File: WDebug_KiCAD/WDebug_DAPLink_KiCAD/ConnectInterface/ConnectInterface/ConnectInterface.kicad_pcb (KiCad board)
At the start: 2 copper layers, 55 x 34 mm, 8 parts, among them J1 Conn_02x05_Counter_Clockwise, J2 Conn_01x20_Female-Connector

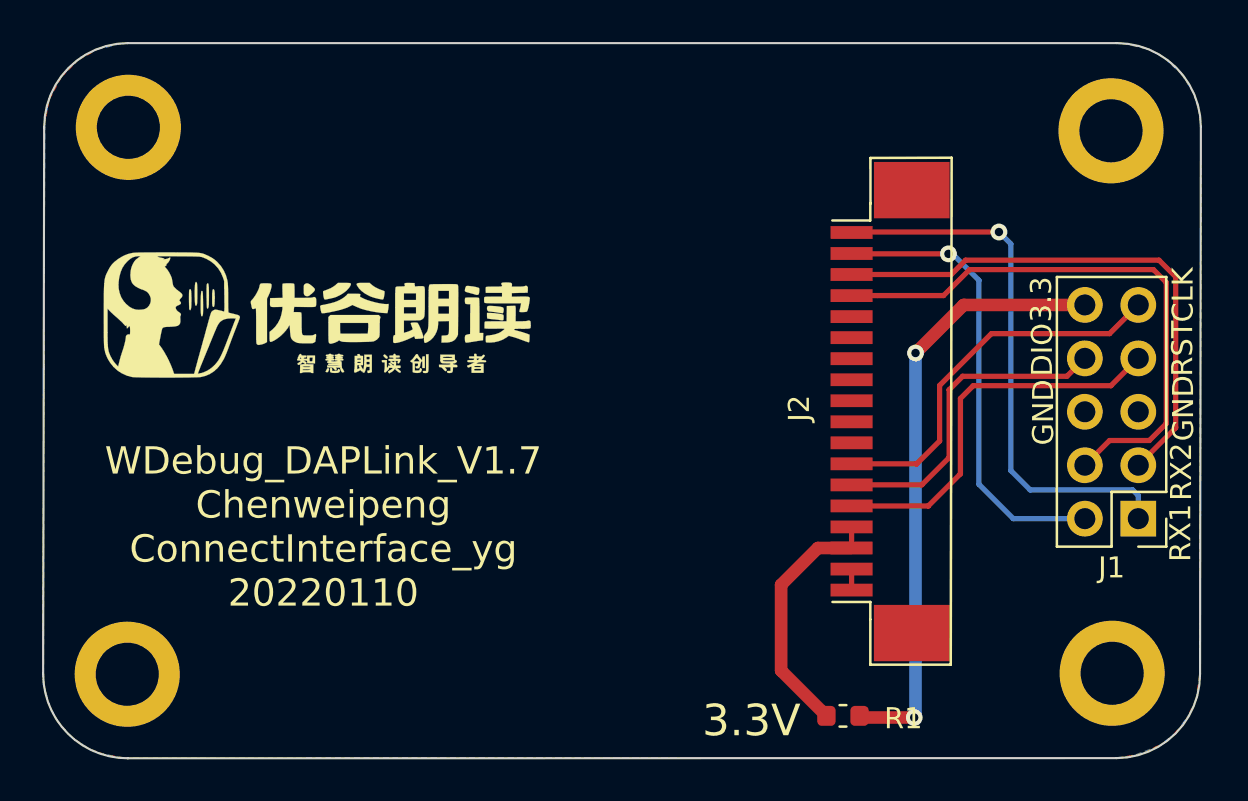
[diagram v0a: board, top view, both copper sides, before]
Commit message: 修改转接板接口定义
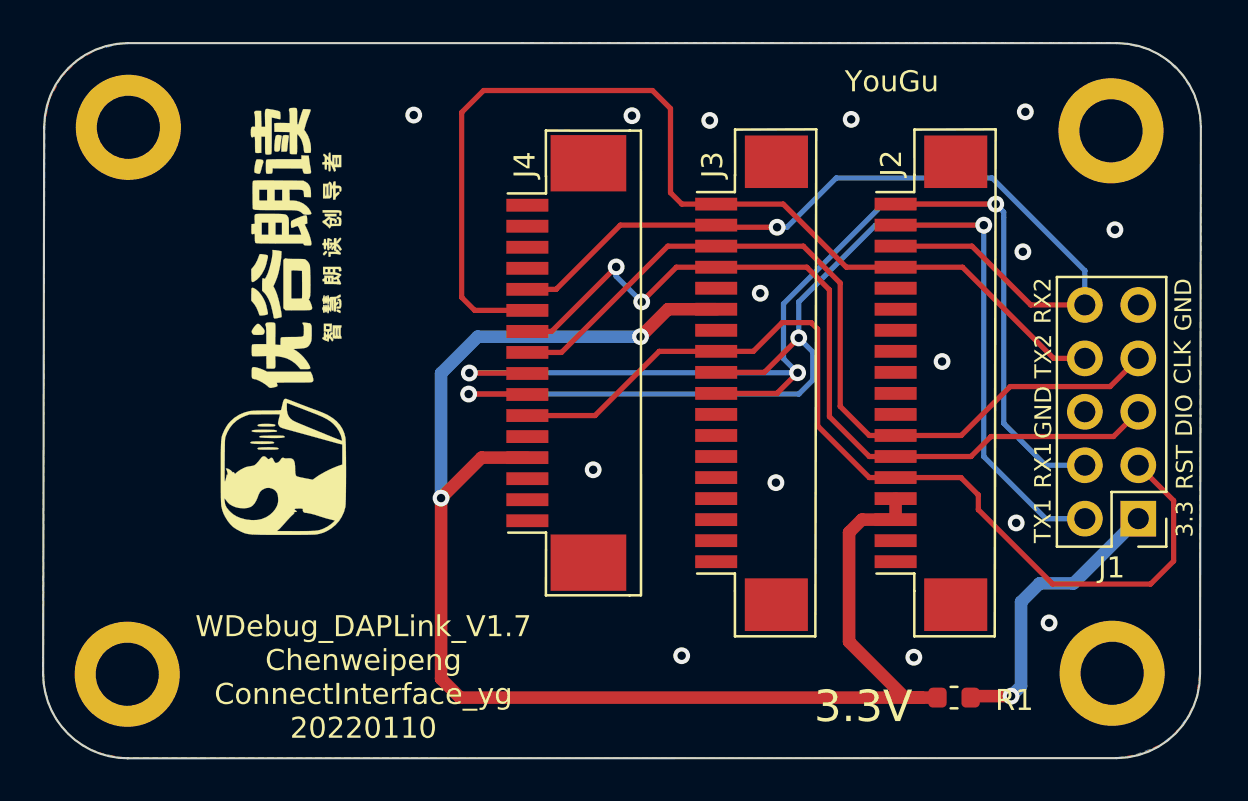
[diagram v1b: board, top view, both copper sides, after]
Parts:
- added J3: Flyaudio18Pin, Connector_PinHeader_1.00mm:1x18_P1.0mm, F.Cu at (166.8, 68.2)
- added J4: Flyaudio16Pin, Connector_PinHeader_1.00mm:1x16_P1.0mm, F.Cu at (154.2, 67.3)
- J1: value Conn_02x05_Counter_Clockwise -> ConnDebug
- J2: value Conn_01x20_Female-Connector -> YOUGU_Debug; footprint WDebug_DAPLink:1x18_P1.0mm -> Connector_PinHeader_1.00mm:1x18_P1.0mm
- moved R1 5.35 mm to (171.8, 83.3)
- moved J2 2.49 mm to (175.3, 68.2)
- moved G*** 2.06 mm to (139.8, 65.1), turned to 90 degrees
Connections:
- net Net-(J2-Pad3) renamed /3_3V
- J1 pad 1: /RX1 -> Net-(J1-Pad1)
- J1 pad 10: Net-(J1-Pad10) -> /RX2
- J1 pad 3: /RX2 -> /TG_RST
- J1 pad 4: /TX2 -> /RX1
- J1 pad 5: GND -> /T_SWDIO
- J1 pad 7: /TG_RST -> /T_SWCLK
- J1 pad 8: /T_SWDIO -> /TX2
- J1 pad 9: /T_SWCLK -> GND
- R1 pad 2: Net-(J1-Pad10) -> Net-(J1-Pad1)
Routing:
- net /3_3V: track 12.2 -> 70.9 mm, vias 0 -> 2
- net /TX1: track 22.0 -> 59.6 mm, vias 1 -> 3
- net /RX1: track 26.2 -> 58.3 mm, vias 1 -> 3
- net Net-(J1-Pad10): track 29.0 -> 0.00 mm, vias 2 -> 0
- net /TG_RST: track 18.6 -> 46.5 mm
- net /T_SWDIO: track 15.5 -> 40.1 mm, vias 0 -> 2
- net /TX2: track 27.2 -> 49.8 mm
- net /T_SWCLK: track 18.3 -> 39.8 mm
- net /RX2: track 25.7 -> 42.4 mm, vias 0 -> 1
- net Net-(J1-Pad1): track 0.00 -> 14.0 mm, vias 0 -> 1
- net GND: track 1.00 -> 0.00 mm, vias 0 -> 15
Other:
- board text added: "TX1"
- board text added: "TX2"
- board text added: "YouGu"

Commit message: 修改V1.7版本 typec元件切换/晶振封装切换/SWD接口切换/新加3.3v调试电阻
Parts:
- renumbered REF** to 1, REF** to 2, REF** to 3, REF** to 4
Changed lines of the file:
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@@
-(kicad_pcb (version 20171130) (host pcbnew "(5.1.9)-1")
+(kicad_pcb (version 20171130) (host pcbnew "(5.1.4)-1")
   (general
     (thickness 1.6)
@@
   (module WDebug_DAPLink:hanpan locked (layer F.Cu)
     (at 132.60578 60.15228)
-    (fp_text reference REF** (at -0.2667 -0.4064) (layer F.SilkS) hide
+    (fp_text reference 4 (at 4.82346 -6.50748) (layer F.SilkS) hide
       (effects (font (size 1 1) (thickness 0.15)))
     )
@@
   (module WDebug_DAPLink:hanpan locked (layer F.Cu)
     (at 132.61848 84.76488)
-    (fp_text reference REF** (at 0 0.5) (layer F.SilkS) hide
+    (fp_text reference 3 (at 0.41402 -6.6294) (layer F.SilkS) hide
       (effects (font (size 1 1) (thickness 0.15)))
     )
-    (fp_text value hanpan (at 0 -0.5) (layer F.Fab)
+    (fp_text value hanpan (at 5.48132 -6.7691) (layer F.Fab)
       (effects (font (size 1 1) (thickness 0.15)))
     )
@@
   (module WDebug_DAPLink:hanpan locked (layer F.Cu)
     (at 179.373812 86.10634)
-    (fp_text reference REF** (at -0.2667 -0.4064) (layer F.SilkS) hide
+    (fp_text reference 2 (at -4.304312 -1.33638) (layer F.SilkS) hide
       (effects (font (size 1 1) (thickness 0.15)))
     )
-    (fp_text value hanpan (at 0 -0.5) (layer F.Fab)
+    (fp_text value hanpan (at 0.770608 -7.54668) (layer F.Fab)
       (effects (font (size 1 1) (thickness 0.15)))
     )
@@
   (module WDebug_DAPLink:hanpan locked (layer F.Cu)
     (at 179.31892 60.31738)
-    (fp_text reference REF** (at -0.2667 -0.4064) (layer F.SilkS) hide
+    (fp_text reference 1 (at -4.43484 -6.21792) (layer F.SilkS) hide
       (effects (font (size 1 1) (thickness 0.15)))
     )

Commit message: 一点修改和生成打样文件
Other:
- board text added: "Flyaudio"
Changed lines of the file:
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@@
   (general
     (thickness 1.6)
-    (drawings 21)
+    (drawings 22)
     (tracks 158)
     (zones 0)
@@
       (drillshape 0)
       (scaleselection 1)
-      (outputdirectory "connectInterface_V1.0/"))
+      (outputdirectory "connectInterface_V1.7/"))
   )
   (net 0 "")
@@
       (net 33 "Net-(J4-Pad15)"))
   )
-  (gr_text YouGu (at 168.86936 53.99024) (layer F.SilkS)
+  (gr_text Flyaudio (at 158.18612 53.467) (layer F.SilkS)
     (effects (font (size 1 1) (thickness 0.2)))
   )
+  (gr_text YouGu (at 170.86834 53.84546) (layer F.SilkS)
+    (effects (font (size 1 1) (thickness 0.2)))
+  )
